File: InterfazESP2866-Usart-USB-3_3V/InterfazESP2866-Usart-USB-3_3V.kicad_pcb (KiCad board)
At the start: 2 copper layers, 41.9 x 32.4 mm, 12 parts, among them P1 USB_USART, P2 ESP2866, P3 Flash, U1 LM1084IS-ADJ/NOPB

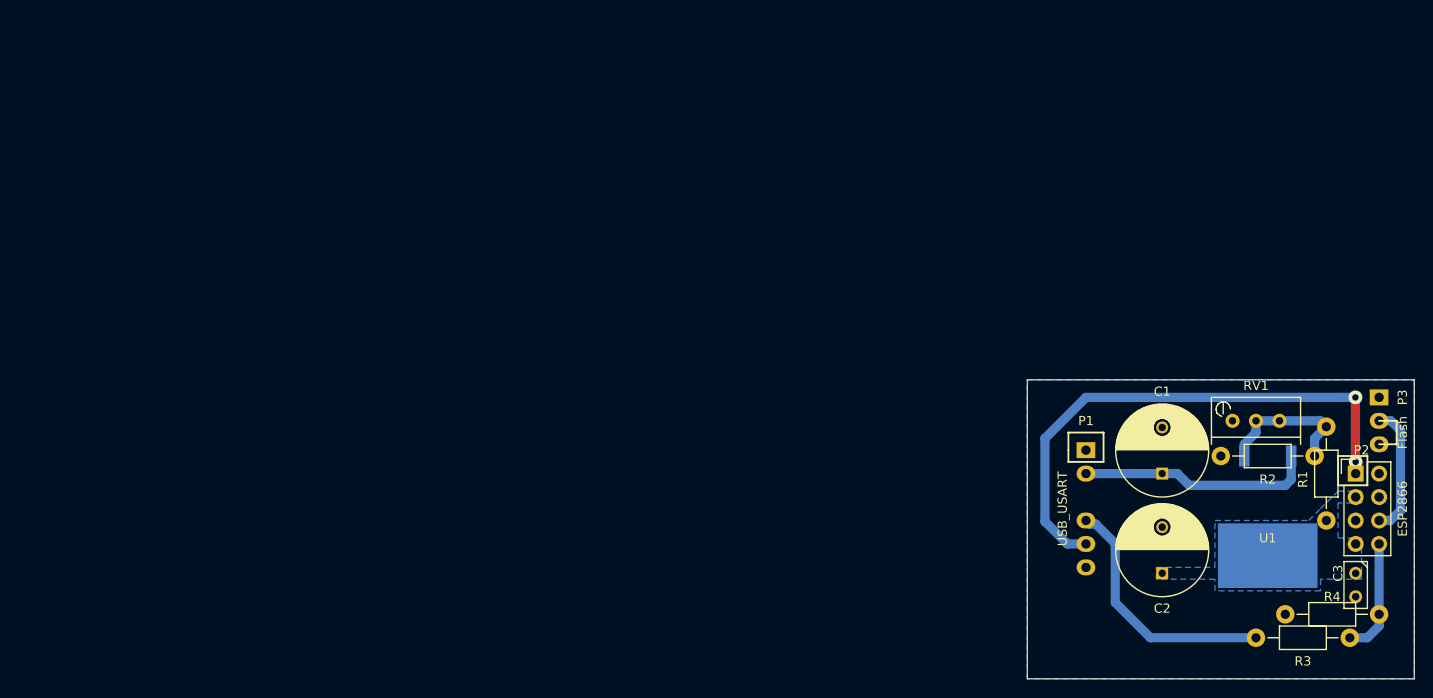
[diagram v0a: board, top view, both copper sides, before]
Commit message: Cambios menores en interfaz usb
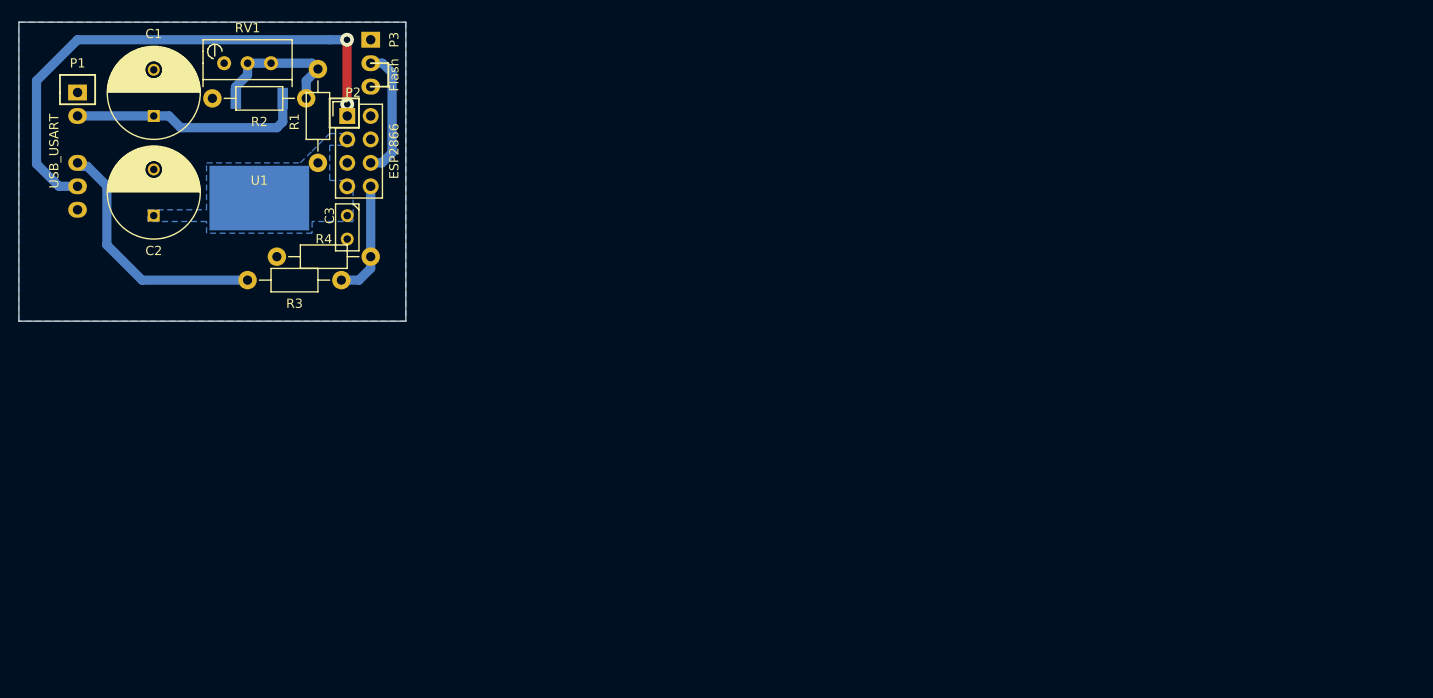
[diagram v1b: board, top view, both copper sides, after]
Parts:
- moved C1 115.9 mm to (34.3, 29.8)
- moved C2 115.9 mm to (34.3, 40.6)
- moved C3 115.9 mm to (55.2, 41.9)
- moved P1 115.9 mm to (26.0, 27.3)
- moved P2 115.9 mm to (55.2, 29.8)
- moved P3 115.9 mm to (57.8, 21.6)
- moved R1 115.9 mm to (52.1, 29.8)
- moved R2 115.9 mm to (45.7, 27.9)
- moved R3 115.9 mm to (49.5, 47.6)
- moved RV1 115.9 mm to (41.9, 24.1)
- moved U1 115.9 mm to (45.7, 27.9)
- moved R4 115.9 mm to (52.7, 45.1)

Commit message: Terminado de rutear interfaz usart usb
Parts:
- P2: value ESP2866 -> ESP8266
- moved C3 0.63 mm to (54.6, 41.9)
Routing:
- net /TXD_USB: track 27.4 -> 28.1 mm
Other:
- net class Default: via_dia 1.5 -> 2
- net class Vcc_USB added: clearance 0.8, trace_width 1.143, via_dia 2, via_drill 0.7
